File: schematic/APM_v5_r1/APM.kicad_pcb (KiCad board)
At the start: 4 copper layers, 72.5 x 104.5 mm, 99 parts, among them J1 DF40C-60DS-0.4V(51), J11 DAC_L_PRB, J12 Conn_01x02, J14 POT_FFC, J16 USB_A_FEMALE, J17 MIDI_DGB, J18 CTRL_FFC, J19 AudioPlug3, J2 CAN, J23 VOL_L_CTRL, J24 VOL_R_CTRL, J3 DF40C-60DS-0.4V(51), J30 UART_DEBUG, J4 LCD_display, J7 DAC_R_PRB, U1 NUCLEO-H753ZI, U13 INA219AxD, U2 OPA1678, U3 LT1963AxST-3.3, U4 W25Q128JVS, U5 MR25H40, U6 W25Q128JVS, U7 INA219AxD, U8 24LC1025-I_P, U9 USBLC6-2SC6

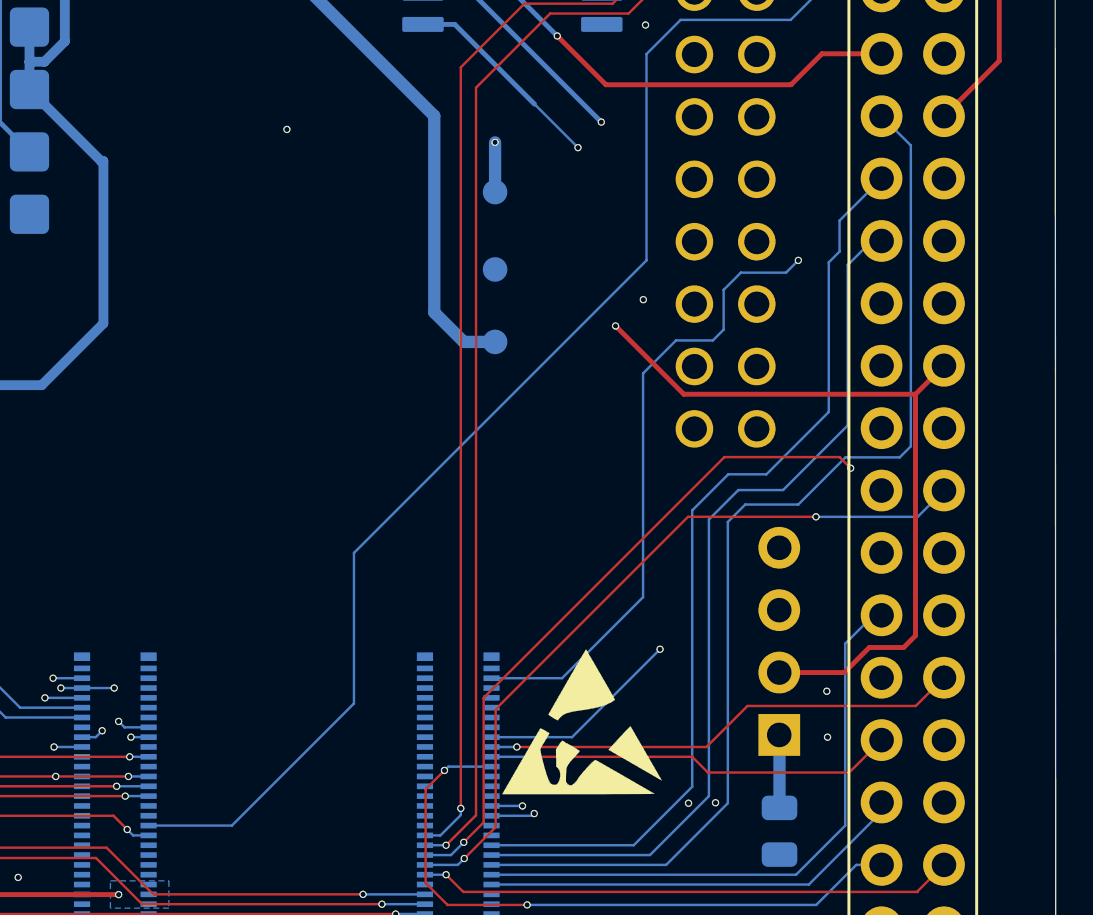
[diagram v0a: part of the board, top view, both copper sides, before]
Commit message: adding renders and render script
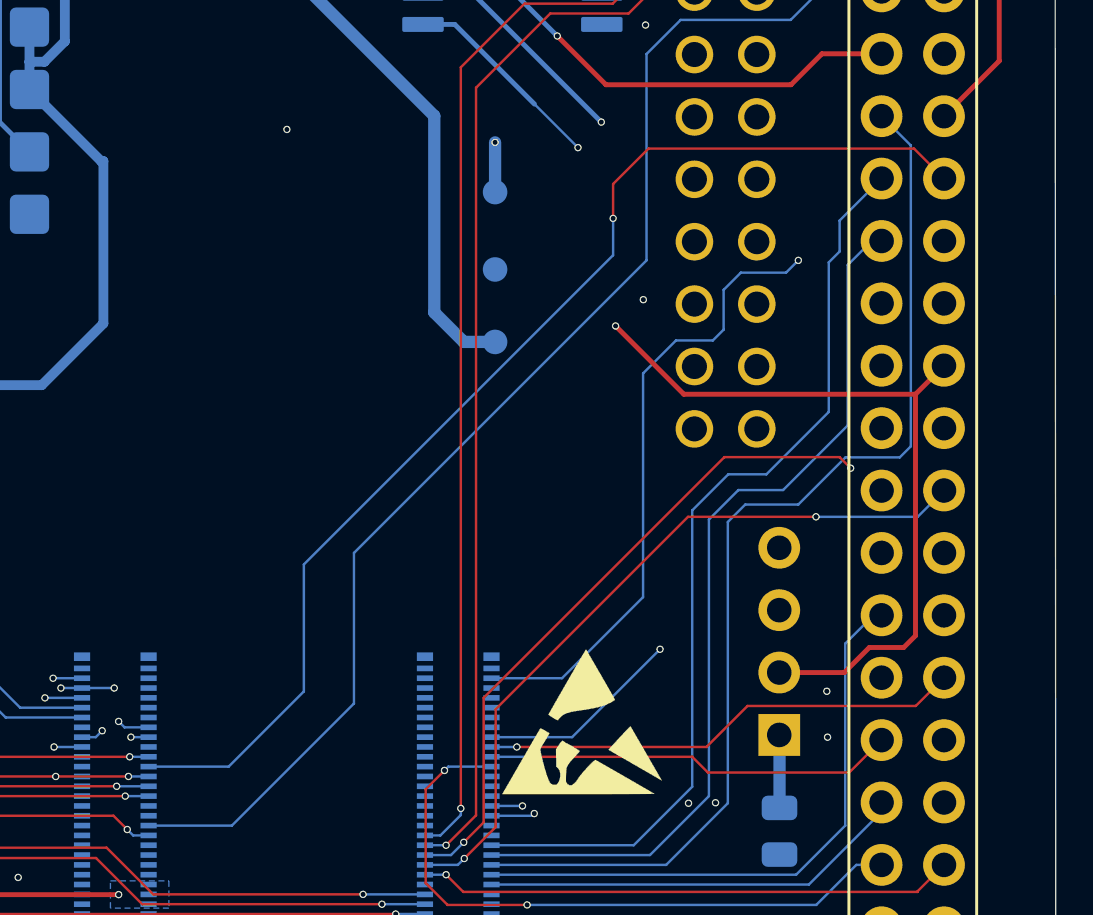
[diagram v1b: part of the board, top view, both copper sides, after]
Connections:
- J3 pad 22: unconnected-(J3-Pin_22-Pad22) -> /APM_FMC_A19
- U1 pad 47: /APM_FMC_19 -> /APM_FMC_A19
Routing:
- net /APM_FMC_A19: track 0.00 -> 48.0 mm, vias 0 -> 1
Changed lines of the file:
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@@
 			(layers "*.Cu" "*.Mask")
 			(remove_unused_layers no)
-			(net "/APM_FMC_19")
+			(net "/APM_FMC_A19")
 			(pinfunction "PE3_47")
 			(pintype "bidirectional")
@@
 			(size 0.23 0.66)
 			(layers "B.Cu" "B.Mask")
-			(net "unconnected-(J3-Pin_22-Pad22)")
+			(net "/APM_FMC_A19")
 			(pinfunction "Pin_22_22")
 			(pintype "passive")
@@
 		(net "/FPGA_INTERFACE/FPGA_3V3")
 	)
+	(segment
+		(start 114.98 121.22)
+		(end 114.98 122.62)
+		(width 0.1)
+		(layer "F.Cu")
+		(net "/APM_FMC_A19")
+	)
+	(segment
+		(start 128.45 121)
+		(end 127.23 119.78)
+		(width 0.1)
+		(layer "F.Cu")
+		(net "/APM_FMC_A19")
+	)
+	(segment
+		(start 116.42 119.78)
+		(end 114.98 121.22)
+		(width 0.1)
+		(layer "F.Cu")
+		(net "/APM_FMC_A19")
+	)
+	(segment
+		(start 127.23 119.78)
+		(end 116.42 119.78)
+		(width 0.1)
+		(layer "F.Cu")
+		(net "/APM_FMC_A19")
+	)
+	(via
+		(at 114.98 122.62)
+		(size 0.3)
+		(drill 0.2)
+		(layers "F.Cu" "B.Cu")
+		(net "/APM_FMC_A19")
+	)
+	(segment
+		(start 102.39 136.71)
+		(end 114.98 124.12)
+		(width 0.1)
+		(layer "B.Cu")
+		(net "/APM_FMC_A19")
+	)
+	(segment
+		(start 102.39 141.88)
+		(end 102.39 136.71)
+		(width 0.1)
+		(layer "B.Cu")
+		(net "/APM_FMC_A19")
+	)
+	(segment
+		(start 114.98 124.12)
+		(end 114.98 122.62)
+		(width 0.1)
+		(layer "B.Cu")
+		(net "/APM_FMC_A19")
+	)
+	(segment
+		(start 99.33 144.94)
+		(end 102.39 141.88)
+		(width 0.1)
+		(layer "B.Cu")
+		(net "/APM_FMC_A19")
+	)
+	(segment
+		(start 96.07 144.94)
+		(end 99.33 144.94)
+		(width 0.1)
+		(layer "B.Cu")
+		(net "/APM_FMC_A19")
+	)
 	(zone

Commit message: schematic for the oscillator board
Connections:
- J3 pad 48: /FPGA_INTERFACE/FPGA_3V3 -> unconnected-(J3-Pin_48-Pad48)
- J3 pad 50: /FPGA_INTERFACE/FPGA_3V3 -> unconnected-(J3-Pin_50-Pad50)
- J3 pad 52: /FPGA_INTERFACE/FPGA_5V -> unconnected-(J3-Pin_52-Pad52)
- J3 pad 54: /FPGA_INTERFACE/FPGA_5V -> unconnected-(J3-Pin_54-Pad54)
- J3 pad 56: /FPGA_INTERFACE/FPGA_5V -> unconnected-(J3-Pin_56-Pad56)
- J3 pad 58: /FPGA_INTERFACE/FPGA_5V -> unconnected-(J3-Pin_58-Pad58)
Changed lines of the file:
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@@
 			(size 0.23 0.66)
 			(layers "B.Cu" "B.Mask")
-			(net "/FPGA_INTERFACE/FPGA_3V3")
+			(net "unconnected-(J3-Pin_48-Pad48)")
 			(pinfunction "Pin_48_48")
-			(pintype "passive")
+			(pintype "passive+no_connect")
 			(solder_mask_margin 0.102)
 		)
@@
 			(size 0.23 0.66)
 			(layers "B.Cu" "B.Mask")
-			(net "/FPGA_INTERFACE/FPGA_3V3")
+			(net "unconnected-(J3-Pin_50-Pad50)")
 			(pinfunction "Pin_50_50")
-			(pintype "passive")
+			(pintype "passive+no_connect")
 			(solder_mask_margin 0.102)
 		)
@@
 			(size 0.23 0.66)
 			(layers "B.Cu" "B.Mask")
-			(net "/FPGA_INTERFACE/FPGA_5V")
+			(net "unconnected-(J3-Pin_52-Pad52)")
 			(pinfunction "Pin_52_52")
-			(pintype "passive")
+			(pintype "passive+no_connect")
 			(solder_mask_margin 0.102)
 		)
@@
 			(size 0.23 0.66)
 			(layers "B.Cu" "B.Mask")
-			(net "/FPGA_INTERFACE/FPGA_5V")
+			(net "unconnected-(J3-Pin_54-Pad54)")
 			(pinfunction "Pin_54_54")
-			(pintype "passive")
+			(pintype "passive+no_connect")
 			(solder_mask_margin 0.102)
 		)
@@
 			(size 0.23 0.66)
 			(layers "B.Cu" "B.Mask")
-			(net "/FPGA_INTERFACE/FPGA_5V")
+			(net "unconnected-(J3-Pin_56-Pad56)")
 			(pinfunction "Pin_56_56")
-			(pintype "passive")
+			(pintype "passive+no_connect")
 			(solder_mask_margin 0.102)
 		)
@@
 			(size 0.23 0.66)
 			(layers "B.Cu" "B.Mask")
-			(net "/FPGA_INTERFACE/FPGA_5V")
+			(net "unconnected-(J3-Pin_58-Pad58)")
 			(pinfunction "Pin_58_58")
-			(pintype "passive")
+			(pintype "passive+no_connect")
 			(solder_mask_margin 0.102)
 		)
@@
 			(net "/FPGA_INTERFACE/FPGA_5V")
 			(pinfunction "Pin_60_60")
-			(pintype "passive")
+			(pintype "passive+no_connect")
 			(solder_mask_margin 0.102)
 		)
